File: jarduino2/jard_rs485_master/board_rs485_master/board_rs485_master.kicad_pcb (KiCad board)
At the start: 2 copper layers, 132.4 x 70.8 mm, 57 parts, among them J1 POWER_12V, J2 Log, J3 POWER_OYAS_12V, J4 BUS_OYAS, J5 Leds RGB, J6 Button, J7 Adapt BUS, Q1 BPC_2N2222A, Q2 P03P4L-04, Q3 BC327, Q4 BC327, U1 RtcArduino, U2 BPC_Alim5V, U3 BPC_ESP8266-01_ESP-01, U4 BPC_Mod485, U5 LM1117DT-3.3

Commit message: Marquage date
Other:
- board text added: "24/04/2024"
- board text removed: "09/04/2024"
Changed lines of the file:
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@@
   (title_block
     (title "Commande des OYAs - Maître RS485 - \"Maître des OYAs\"")
-    (date "2024-04-09")
+    (date "2024-04-24")
     (rev "B0")
     (company "BPC")
@@
     (effects (font (size 1.4 1.4) (thickness 0.3) bold) (justify left bottom))
   )
-  (gr_text "09/04/2024" (at 180.89 118.05 40) (layer "F.SilkS")
+  (gr_text "24/04/2024" (at 180.89 118.05 40) (layer "F.SilkS")
     (effects (font (size 0.8 0.8) (thickness 0.1)) (justify left bottom))
   )

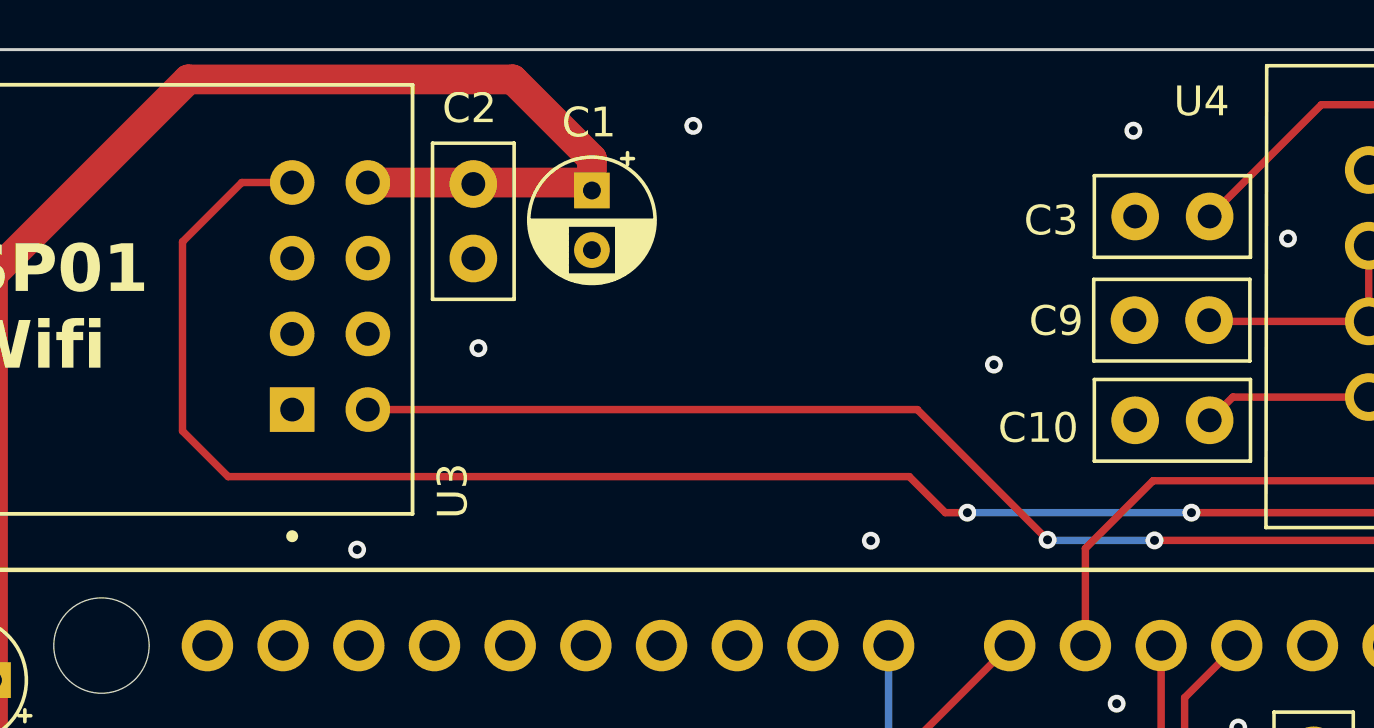
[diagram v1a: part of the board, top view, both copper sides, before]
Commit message: Correction de l'inversion RX/TX du module Wifi
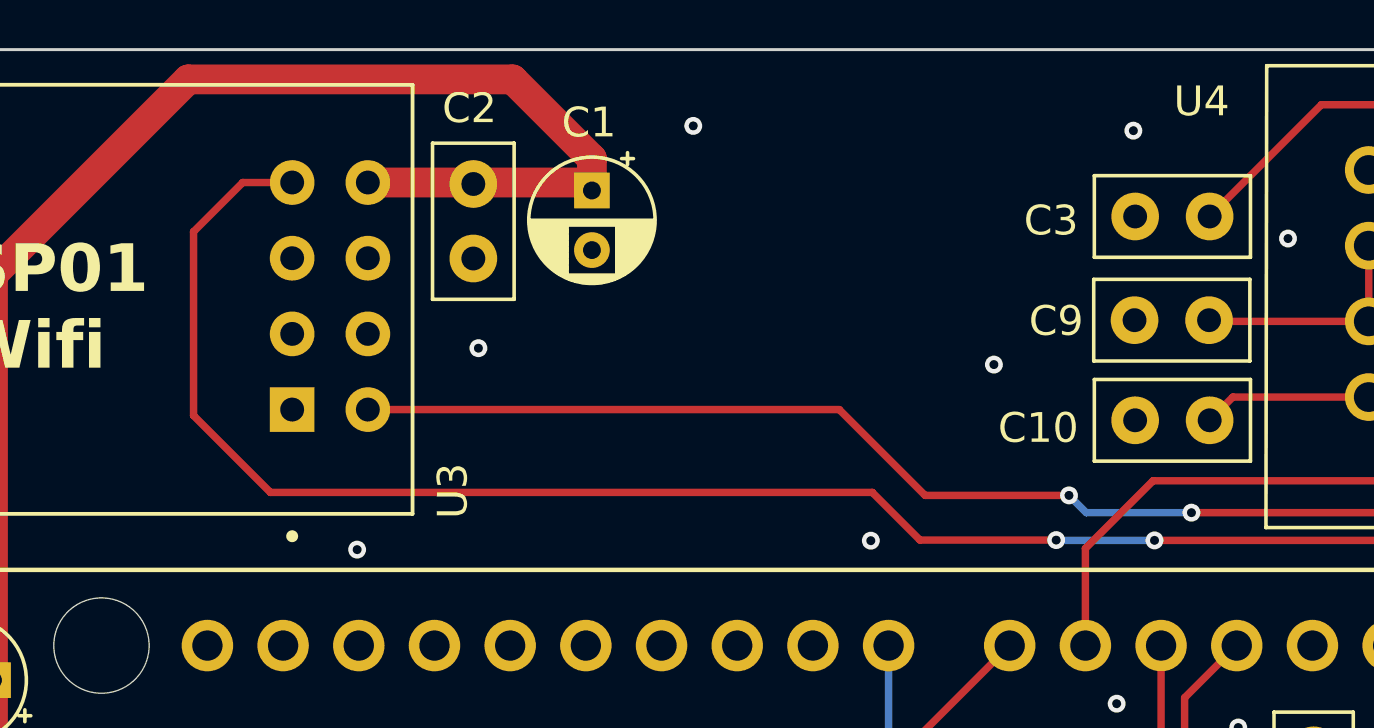
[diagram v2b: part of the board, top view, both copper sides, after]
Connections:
- U3 pad 4: RX_WIFI -> TX_WIFI
- U3 pad 5: TX_WIFI -> RX_WIFI
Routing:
- net RX_WIFI: track 73.0 -> 56.3 mm
- net TX_WIFI: track 53.7 -> 69.6 mm
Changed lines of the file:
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@@
       (net 101 "unconnected-(U3-IO0-Pad3)") (pinfunction "IO0") (pintype "bidirectional+no_connect"))
     (pad "4" thru_hole circle (at 3.81 8.31 90) (size 1.5 1.5) (drill 0.8) (layers "*.Cu" "*.Mask")
-      (net 100 "RX_WIFI") (pinfunction "RXD") (pintype "input"))
+      (net 103 "TX_WIFI") (pinfunction "RXD") (pintype "input"))
     (pad "5" thru_hole circle (at -3.81 10.85 90) (size 1.5 1.5) (drill 0.8) (layers "*.Cu" "*.Mask")
-      (net 103 "TX_WIFI") (pinfunction "TXD") (pintype "output"))
+      (net 100 "RX_WIFI") (pinfunction "TXD") (pintype "output"))
     (pad "6" thru_hole circle (at -1.27 10.85 90) (size 1.5 1.5) (drill 0.8) (layers "*.Cu" "*.Mask")
       (net 104 "unconnected-(U3-EN-Pad6)") (pinfunction "EN") (pintype "input+no_connect"))
@@
   (segment (start 105.18 76.81) (end 103.18 78.81) (width 0.25) (layer "F.Cu") (net 99))
   (segment (start 112.49 76.81) (end 105.18 76.81) (width 0.25) (layer "F.Cu") (net 99))
-  (segment (start 116.93 63.33) (end 94.07 63.33) (width 0.25) (layer "F.Cu") (net 100))
-  (segment (start 94.53 53.46) (end 96.22 53.46) (width 0.25) (layer "F.Cu") (net 100))
+  (segment (start 114.58 61.08) (end 98.76 61.08) (width 0.25) (layer "F.Cu") (net 100))
   (segment (start 150.78 67.35) (end 147.97 64.54) (width 0.25) (layer "F.Cu") (net 100))
-  (segment (start 94.07 63.33) (end 92.54 61.8) (width 0.25) (layer "F.Cu") (net 100))
-  (segment (start 118.14 64.54) (end 116.93 63.33) (width 0.25) (layer "F.Cu") (net 100))
   (segment (start 150.78 69) (end 150.78 67.35) (width 0.25) (layer "F.Cu") (net 100))
   (segment (start 147.97 64.54) (end 126.4 64.54) (width 0.25) (layer "F.Cu") (net 100))
-  (segment (start 92.54 55.45) (end 94.53 53.46) (width 0.25) (layer "F.Cu") (net 100))
-  (segment (start 118.88 64.54) (end 118.14 64.54) (width 0.25) (layer "F.Cu") (net 100))
-  (segment (start 92.54 61.8) (end 92.54 55.45) (width 0.25) (layer "F.Cu") (net 100))
-  (via (at 118.88 64.54) (size 0.6) (drill 0.3) (layers "F.Cu" "B.Cu") (net 100))
+  (segment (start 117.46 63.96) (end 114.58 61.08) (width 0.25) (layer "F.Cu") (net 100))
+  (segment (start 122.29 63.96) (end 117.46 63.96) (width 0.25) (layer "F.Cu") (net 100))
+  (via (at 122.29 63.96) (size 0.6) (drill 0.3) (layers "F.Cu" "B.Cu") (net 100))
   (via (at 126.4 64.54) (size 0.6) (drill 0.3) (layers "F.Cu" "B.Cu") (net 100))
-  (segment (start 126.4 64.54) (end 118.88 64.54) (width 0.25) (layer "B.Cu") (net 100))
+  (segment (start 122.87 64.54) (end 122.29 63.96) (width 0.25) (layer "B.Cu") (net 100))
+  (segment (start 126.4 64.54) (end 122.87 64.54) (width 0.25) (layer "B.Cu") (net 100))
   (segment (start 148.24 67.48) (end 148.24 69) (width 0.25) (layer "F.Cu") (net 103))
-  (segment (start 121.57 65.45) (end 117.2 61.08) (width 0.25) (layer "F.Cu") (net 103))
+  (segment (start 92.91 55.11) (end 92.91 61.28) (width 0.25) (layer "F.Cu") (net 103))
+  (segment (start 92.91 61.28) (end 95.49 63.86) (width 0.25) (layer "F.Cu") (net 103))
+  (segment (start 115.69 63.86) (end 117.29 65.46) (width 0.25) (layer "F.Cu") (net 103))
+  (segment (start 95.49 63.86) (end 115.69 63.86) (width 0.25) (layer "F.Cu") (net 103))
+  (segment (start 117.29 65.46) (end 121.86 65.46) (width 0.25) (layer "F.Cu") (net 103))
   (segment (start 125.16 65.47) (end 146.23 65.47) (width 0.25) (layer "F.Cu") (net 103))
-  (segment (start 117.2 61.08) (end 98.76 61.08) (width 0.25) (layer "F.Cu") (net 103))
+  (segment (start 94.56 53.46) (end 92.91 55.11) (width 0.25) (layer "F.Cu") (net 103))
   (segment (start 146.23 65.47) (end 148.24 67.48) (width 0.25) (layer "F.Cu") (net 103))
-  (via (at 121.57 65.45) (size 0.6) (drill 0.3) (layers "F.Cu" "B.Cu") (net 103))
+  (segment (start 96.22 53.46) (end 94.56 53.46) (width 0.25) (layer "F.Cu") (net 103))
   (via (at 125.16 65.47) (size 0.6) (drill 0.3) (layers "F.Cu" "B.Cu") (net 103))
-  (segment (start 125.16 65.47) (end 121.59 65.47) (width 0.25) (layer "B.Cu") (net 103))
-  (segment (start 121.59 65.47) (end 121.57 65.45) (width 0.25) (layer "B.Cu") (net 103))
+  (via (at 121.86 65.46) (size 0.6) (drill 0.3) (layers "F.Cu" "B.Cu") (net 103))
+  (segment (start 121.87 65.47) (end 121.86 65.46) (width 0.25) (layer "B.Cu") (net 103))
+  (segment (start 125.16 65.47) (end 121.87 65.47) (width 0.25) (layer "B.Cu") (net 103))
   (zone (net 2) (net_name "GND") (layers "F&B.Cu") (hatch edge 0.5)
     (connect_pads (clearance 0.5))

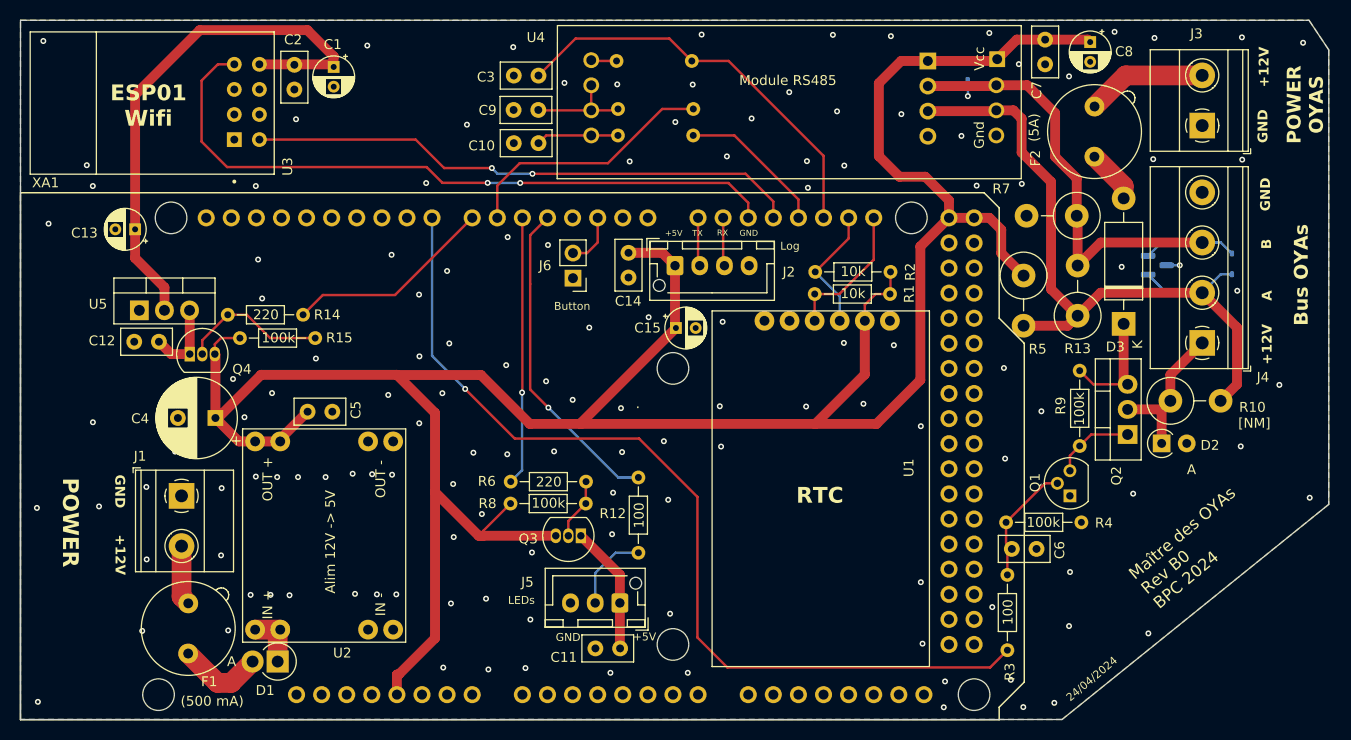
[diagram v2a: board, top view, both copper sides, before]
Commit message: Changement de la logique de commande des PWR Wifi et LEDs (avec un npn en plus)
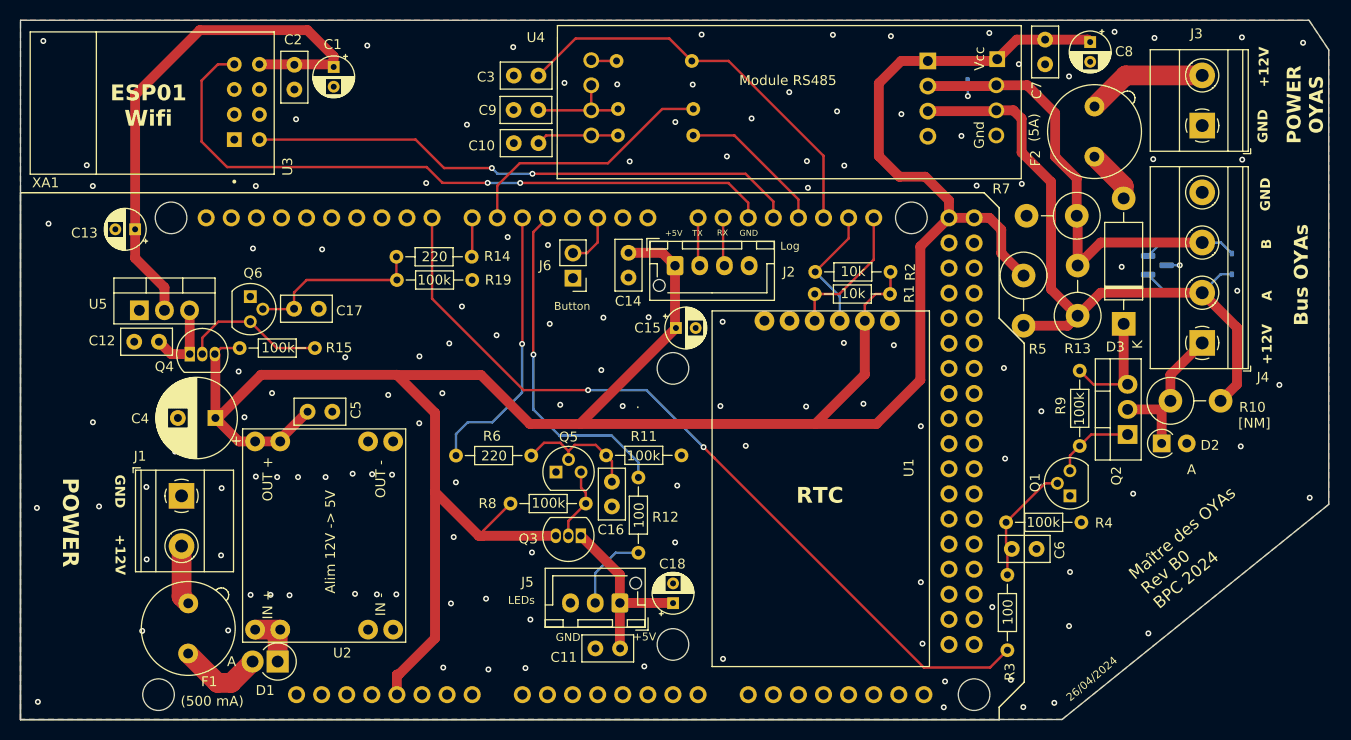
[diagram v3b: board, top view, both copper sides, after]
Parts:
- added C16: 100nF, Capacitor_THT:C_Disc_D5.0mm_W2.5mm_P2.50mm, F.Cu at (134.4, 95.7)
- added C17: 100nF, Capacitor_THT:C_Disc_D5.0mm_W2.5mm_P2.50mm, F.Cu at (102.3, 78.2)
- added C18: 10µF, Capacitor_THT:CP_Radial_D4.0mm_P2.00mm, F.Cu at (140.6, 108.0)
- added Q5: BPC_2N2222A, Package_TO_SOT_THT:TO-92, F.Cu at (128.8, 94.7)
- added Q6: BPC_2N2222A, Package_TO_SOT_THT:TO-92, F.Cu at (97.8, 77.0)
- added R11: 100k, Resistor_THT:R_Axial_DIN0204_L3.6mm_D1.6mm_P7.62mm_Horizontal, F.Cu at (133.9, 93.0)
- added R19: 100k, Resistor_THT:R_Axial_DIN0204_L3.6mm_D1.6mm_P7.62mm_Horizontal, F.Cu at (112.7, 75.3)
- moved R14 18.1 mm to (120.2, 72.9)
- moved R6 6.14 mm to (118.7, 93.1)
- moved R15 1.01 mm to (96.8, 82.2)
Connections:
- R14 pad 2: Net-(Q4-B) -> Net-(C17-Pad1)
- R6 pad 2: Net-(Q3-B) -> Net-(C16-Pad1)
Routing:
- net Net-(C17-Pad1): track 0.00 -> 18.1 mm
- net CMD_WIFI_PWR: track 21.2 -> 3.96 mm
- net Net-(C16-Pad1): track 0.00 -> 12.9 mm
- net CMD_OYAS_PWR: track 94.3 -> 82.6 mm, vias 1 -> 2
- net Net-(J5-Pin_1): track 13.0 -> 18.4 mm
- net DATA_LEDS: track 32.7 -> 34.4 mm
- net Net-(Q3-B): track 6.22 -> 7.38 mm
- net CMD_LEDS_PWR: track 27.2 -> 28.3 mm
- net +5V: track 271.3 -> 270.2 mm
- net GND: vias 136 -> 127
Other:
- board text added: "100k"
- board text added: "26/04/2024"
- board text removed: "24/04/2024"

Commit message: Titres + finitions (vias)
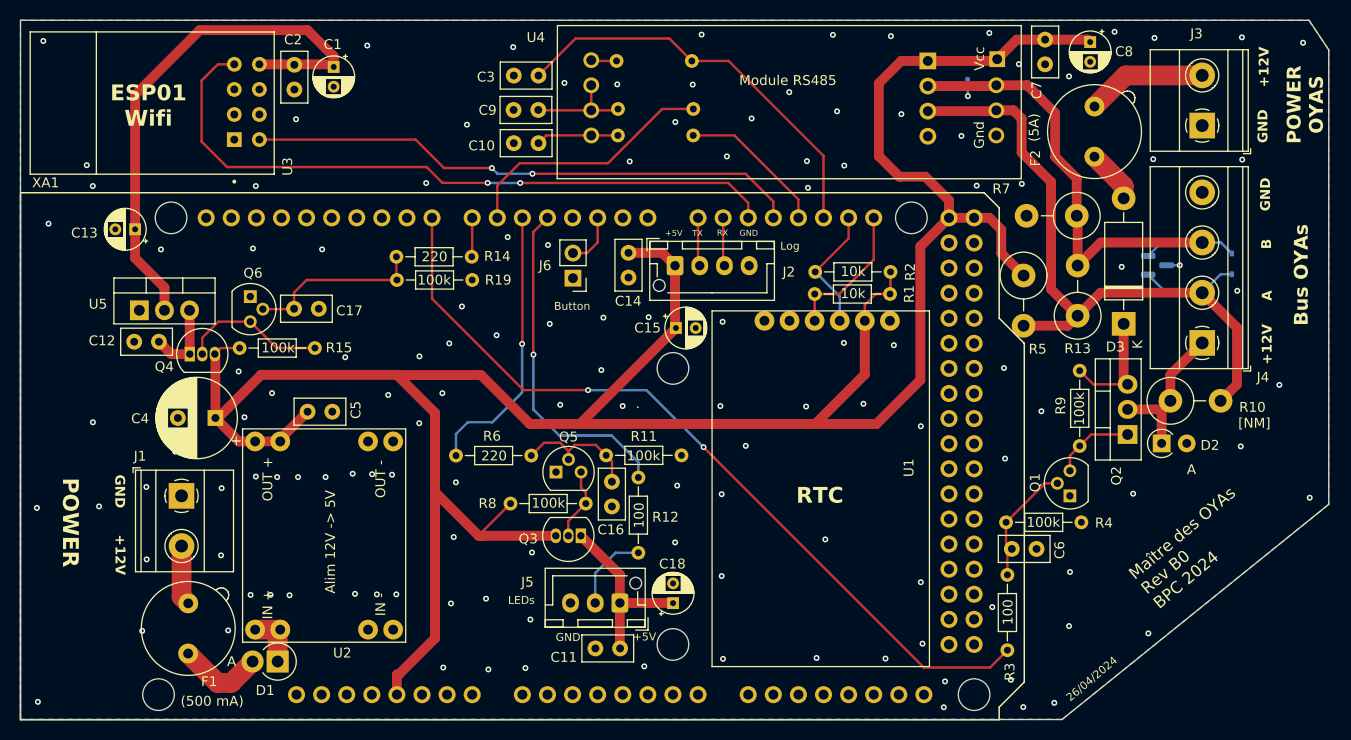
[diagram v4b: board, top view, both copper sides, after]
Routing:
- net GND: vias 127 -> 133
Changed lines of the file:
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@@
   (via (at 174.24 93.37) (size 0.6) (drill 0.3) (layers "F.Cu" "B.Cu") (free) (net 2))
   (via (at 154.18 63.26) (size 0.6) (drill 0.3) (layers "F.Cu" "B.Cu") (free) (net 2))
+  (via (at 162.13 113.61) (size 0.6) (drill 0.3) (layers "F.Cu" "B.Cu") (free) (net 2))
   (via (at 112.62 107.11) (size 0.6) (drill 0.3) (layers "F.Cu" "B.Cu") (free) (net 2))
   (via (at 102.67 95.24) (size 0.6) (drill 0.3) (layers "F.Cu" "B.Cu") (free) (net 2))
@@
   (via (at 100.56 95.24) (size 0.6) (drill 0.3) (layers "F.Cu" "B.Cu") (free) (net 2))
   (via (at 180.81 104.85) (size 0.6) (drill 0.3) (layers "F.Cu" "B.Cu") (free) (net 2))
+  (via (at 145.55 105.26) (size 0.6) (drill 0.3) (layers "F.Cu" "B.Cu") (free) (net 2))
   (via (at 176.08 118.52) (size 0.6) (drill 0.3) (layers "F.Cu" "B.Cu") (free) (net 2))
   (via (at 191.92 73.8) (size 0.6) (drill 0.3) (layers "F.Cu" "B.Cu") (net 2))
@@
   (via (at 123.89 70.95) (size 0.6) (drill 0.3) (layers "F.Cu" "B.Cu") (free) (net 2))
   (via (at 171.36 65.74) (size 0.6) (drill 0.3) (layers "F.Cu" "B.Cu") (free) (net 2))
+  (via (at 156.04 101.55) (size 0.6) (drill 0.3) (layers "F.Cu" "B.Cu") (free) (net 2))
   (via (at 170.47 56.68) (size 0.6) (drill 0.3) (layers "F.Cu" "B.Cu") (net 2))
   (via (at 90.23 92.66) (size 0.6) (drill 0.3) (layers "F.Cu" "B.Cu") (free) (net 2))
@@
   (via (at 143.52 50.45) (size 0.6) (drill 0.3) (layers "F.Cu" "B.Cu") (free) (net 2))
   (via (at 145.69 113.64) (size 0.6) (drill 0.3) (layers "F.Cu" "B.Cu") (free) (net 2))
+  (via (at 145.55 96.97) (size 0.6) (drill 0.3) (layers "F.Cu" "B.Cu") (free) (net 2))
   (via (at 145.42 88.05) (size 0.6) (drill 0.3) (layers "F.Cu" "B.Cu") (free) (net 2))
   (via (at 133.37 84.41) (size 0.6) (drill 0.3) (layers "F.Cu" "B.Cu") (free) (net 2))
@@
   (via (at 165.71 90.09) (size 0.6) (drill 0.3) (layers "F.Cu" "B.Cu") (free) (net 2))
   (via (at 189.36 50.79) (size 0.6) (drill 0.3) (layers "F.Cu" "B.Cu") (free) (net 2))
+  (via (at 88.8 72.2) (size 0.6) (drill 0.3) (layers "F.Cu" "B.Cu") (free) (net 2))
   (via (at 168.16 115.92) (size 0.6) (drill 0.3) (layers "F.Cu" "B.Cu") (free) (net 2))
   (via (at 172.94 108.4) (size 0.6) (drill 0.3) (layers "F.Cu" "B.Cu") (free) (net 2))
@@
   (via (at 140.84 101.85) (size 0.6) (drill 0.3) (layers "F.Cu" "B.Cu") (free) (net 2))
   (via (at 112.19 95) (size 0.6) (drill 0.3) (layers "F.Cu" "B.Cu") (free) (net 2))
+  (via (at 155.16 113.55) (size 0.6) (drill 0.3) (layers "F.Cu" "B.Cu") (free) (net 2))
   (via (at 165.71 105.88) (size 0.6) (drill 0.3) (layers "F.Cu" "B.Cu") (free) (net 2))
   (segment (start 170.47 55.07) (end 170.44 55.04) (width 0.25) (layer "B.Cu") (net 2))
